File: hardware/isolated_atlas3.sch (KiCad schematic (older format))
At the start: 15 parts, among them J501 CONN_01X02, P5 ATLAS_DO_PROBE, U501 ADM3260, U502 ATLAS_DO

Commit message: Trying out some test points.
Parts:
- added J15, J16: CONN_01x02, conservify:TP_Pads_D1.5mm_1x2, symbol conservify:CONN_01x02
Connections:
- wire segments 78 -> 82
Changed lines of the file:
@@
 NoConn ~ 3650 3000
 NoConn ~ 5200 3000
+Text Label 8350 4500 0    60   ~ 0
+ISO_GND
+Text Label 8350 4400 0    60   ~ 0
+ISO_VCC
+Text Label 8350 4150 0    60   ~ 0
+ISO_SCL
+Text Label 8350 4250 0    60   ~ 0
+ISO_SDA
+Wire Wire Line
+	8350 4150 8750 4150
+Wire Wire Line
+	8750 4250 8350 4250
+Wire Wire Line
+	8350 4400 8750 4400
+Wire Wire Line
+	8750 4500 8350 4500
+$Comp
+L conservify:CONN_01x02 J?
+U 1 1 5C0F07A8
+P 8950 4150
+AR Path="/594C282A/5C0F07A8" Ref="J?"  Part="1"
+AR Path="/594C282C/5C0F07A8" Ref="J15"  Part="1"
+F 0 "J15" H 9029 4142 50  0000 L CNN
+F 1 "CONN_01x02" H 9029 4051 50  0000 L CNN
+F 2 "conservify:TP_Pads_D1.5mm_1x2" H 8950 4150 50  0001 C CNN
+F 3 "" H 8950 4150 50  0001 C CNN
+	1    8950 4150
+	1    0    0    -1
+$EndComp
+$Comp
+L conservify:CONN_01x02 J?
+U 1 1 5C0F07AF
+P 8950 4400
+AR Path="/594C282A/5C0F07AF" Ref="J?"  Part="1"
+AR Path="/594C282C/5C0F07AF" Ref="J16"  Part="1"
+F 0 "J16" H 9029 4392 50  0000 L CNN
+F 1 "CONN_01x02" H 9029 4301 50  0000 L CNN
+F 2 "conservify:TP_Pads_D1.5mm_1x2" H 8950 4400 50  0001 C CNN
+F 3 "" H 8950 4400 50  0001 C CNN
+	1    8950 4400
+	1    0    0    -1
+$EndComp
 $EndSCHEMATC

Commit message: Add orientation indicator to SWD fp.
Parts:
- J15, J16: Critical (none) -> (none); MFN (none) -> (none); MFP (none) -> (none); Notes (none) -> (none); Package (none) -> (none); SPN1 (none) -> (none); Source (none) -> ANY; Subsystem (none) -> (none); Supplier1 (none) -> (none)
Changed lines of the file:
@@
+	1    0    0    -1
+$EndComp
+$Comp
+L conservify:CONN_01x02 J?
+U 1 1 5C0F07A8
+P 8950 4150
+AR Path="/594C282A/5C0F07A8" Ref="J?"  Part="1"
+AR Path="/594C282C/5C0F07A8" Ref="J15"  Part="1"
+F 0 "J15" H 9029 4142 50  0000 L CNN
+F 1 "CONN_01x02" H 9029 4051 50  0000 L CNN
+F 2 "conservify:TP_Pads_D1.5mm_1x2" H 8950 4150 50  0001 C CNN
+F 3 "" H 8950 4150 50  0001 C CNN
+F 4 " " H 9029 4242 50  0001 C CNN "Critical"
+F 5 " " H 9029 4242 50  0001 C CNN "MFN"
+F 6 " " H 9029 4242 50  0001 C CNN "MFP"
+F 7 " " H 9029 4242 50  0001 C CNN "Notes"
+F 8 " " H 9029 4242 50  0001 C CNN "Package"
+F 9 " " H 9029 4242 50  0001 C CNN "SPN1"
+F 10 "ANY" H 9029 4242 50  0001 C CNN "Source"
+F 11 " " H 9029 4242 50  0001 C CNN "Subsystem"
+F 12 " " H 9029 4242 50  0001 C CNN "Supplier1"
+	1    8950 4150
+	1    0    0    -1
+$EndComp
+$Comp
+L conservify:CONN_01x02 J?
+U 1 1 5C0F07AF
+P 8950 4400
+AR Path="/594C282A/5C0F07AF" Ref="J?"  Part="1"
+AR Path="/594C282C/5C0F07AF" Ref="J16"  Part="1"
+F 0 "J16" H 9029 4392 50  0000 L CNN
+F 1 "CONN_01x02" H 9029 4301 50  0000 L CNN
+F 2 "conservify:TP_Pads_D1.5mm_1x2" H 8950 4400 50  0001 C CNN
+F 3 "" H 8950 4400 50  0001 C CNN
+F 4 " " H 9029 4492 50  0001 C CNN "Critical"
+F 5 " " H 9029 4492 50  0001 C CNN "MFN"
+F 6 " " H 9029 4492 50  0001 C CNN "MFP"
+F 7 " " H 9029 4492 50  0001 C CNN "Notes"
+F 8 " " H 9029 4492 50  0001 C CNN "Package"
+F 9 " " H 9029 4492 50  0001 C CNN "SPN1"
+F 10 "ANY" H 9029 4492 50  0001 C CNN "Source"
+F 11 " " H 9029 4492 50  0001 C CNN "Subsystem"
+F 12 " " H 9029 4492 50  0001 C CNN "Supplier1"
+	1    8950 4400
 	1    0    0    -1
 $EndComp
@@
 Text Label 9450 2900 0    60   ~ 0
 DO_PGND
+Text Label 8350 4500 0    60   ~ 0
+ISO_GND
+Text Label 8350 4400 0    60   ~ 0
+ISO_VCC
+Text Label 8350 4150 0    60   ~ 0
+ISO_SCL
+Text Label 8350 4250 0    60   ~ 0
+ISO_SDA
 Wire Wire Line
 	5200 3300 5350 3300
@@
 Wire Wire Line
 	6900 2500 7400 2500
+Wire Wire Line
+	8350 4150 8750 4150
+Wire Wire Line
+	8750 4250 8350 4250
+Wire Wire Line
+	8350 4400 8750 4400
+Wire Wire Line
+	8750 4500 8350 4500
 Connection ~ 5350 3500
 Connection ~ 5350 3400
@@
 NoConn ~ 3650 3000
 NoConn ~ 5200 3000
-Text Label 8350 4500 0    60   ~ 0
-ISO_GND
-Text Label 8350 4400 0    60   ~ 0
-ISO_VCC
-Text Label 8350 4150 0    60   ~ 0
-ISO_SCL
-Text Label 8350 4250 0    60   ~ 0
-ISO_SDA
-Wire Wire Line
-	8350 4150 8750 4150
-Wire Wire Line
-	8750 4250 8350 4250
-Wire Wire Line
-	8350 4400 8750 4400
-Wire Wire Line
-	8750 4500 8350 4500
-$Comp
-L conservify:CONN_01x02 J?
-U 1 1 5C0F07A8
-P 8950 4150
-AR Path="/594C282A/5C0F07A8" Ref="J?"  Part="1"
-AR Path="/594C282C/5C0F07A8" Ref="J15"  Part="1"
-F 0 "J15" H 9029 4142 50  0000 L CNN
-F 1 "CONN_01x02" H 9029 4051 50  0000 L CNN
-F 2 "conservify:TP_Pads_D1.5mm_1x2" H 8950 4150 50  0001 C CNN
-F 3 "" H 8950 4150 50  0001 C CNN
-	1    8950 4150
-	1    0    0    -1
-$EndComp
-$Comp
-L conservify:CONN_01x02 J?
-U 1 1 5C0F07AF
-P 8950 4400
-AR Path="/594C282A/5C0F07AF" Ref="J?"  Part="1"
-AR Path="/594C282C/5C0F07AF" Ref="J16"  Part="1"
-F 0 "J16" H 9029 4392 50  0000 L CNN
-F 1 "CONN_01x02" H 9029 4301 50  0000 L CNN
-F 2 "conservify:TP_Pads_D1.5mm_1x2" H 8950 4400 50  0001 C CNN
-F 3 "" H 8950 4400 50  0001 C CNN
-	1    8950 4400
-	1    0    0    -1
-$EndComp
 $EndSCHEMATC

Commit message: Started transition to 4 layer board
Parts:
- removed J15, J16: CONN_01x02, conservify:TP_Pads_D1.5mm_1x2, symbol conservify:CONN_01x02
- C501, C502, C503, C504, C505, C506: symbol conservify:CAPACITOR_CERAMIC -> fk-atlas-rescue:CAPACITOR_CERAMIC-conservify
- J501: symbol conservify:CONN_01x02 -> fk-atlas-rescue:CONN_01x02-conservify
- P5: symbol conservify:ATLAS_WATER_PROBE -> fk-atlas-rescue:ATLAS_WATER_PROBE-conservify
- R501, R502, R503, R504, R505: symbol conservify:R -> fk-atlas-rescue:R-conservify
- U501: symbol conservify:ADM3260 -> fk-atlas-rescue:ADM3260-conservify
- U502: footprint conservify:ATLAS_SENSOR_BOARD_OEM -> conservify:ATLAS_SENSOR_BOARD_COMBO; symbol conservify:ATLAS_SENSOR -> fk-atlas-rescue:ATLAS_SENSOR-conservify
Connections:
- wire segments 82 -> 78
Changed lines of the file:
@@
 $EndDescr
 $Comp
-L conservify:ADM3260 U501
+L fk-atlas-rescue:ADM3260-conservify U501
 U 1 1 594C2CF0
 P 4400 2900
@@
 $EndComp
 $Comp
-L conservify:CAPACITOR_CERAMIC C503
+L fk-atlas-rescue:CAPACITOR_CERAMIC-conservify C503
 U 1 1 594C2CF5
 P 5650 3800
@@
 $EndComp
 $Comp
-L conservify:CAPACITOR_CERAMIC C504
+L fk-atlas-rescue:CAPACITOR_CERAMIC-conservify C504
 U 1 1 594C2CF9
 P 5650 4100
@@
 $EndComp
 $Comp
-L conservify:CAPACITOR_CERAMIC C505
+L fk-atlas-rescue:CAPACITOR_CERAMIC-conservify C505
 U 1 1 594C2CFC
 P 5650 4400
@@
 $EndComp
 $Comp
-L conservify:CAPACITOR_CERAMIC C506
+L fk-atlas-rescue:CAPACITOR_CERAMIC-conservify C506
 U 1 1 594C2D00
 P 5650 4650
@@
 $EndComp
 $Comp
-L conservify:CAPACITOR_CERAMIC C501
+L fk-atlas-rescue:CAPACITOR_CERAMIC-conservify C501
 U 1 1 5948D5F5
 P 2900 3800
@@
 $EndComp
 $Comp
-L conservify:CAPACITOR_CERAMIC C502
+L fk-atlas-rescue:CAPACITOR_CERAMIC-conservify C502
 U 1 1 5948D68D
 P 2900 4100
@@
 $EndComp
 $Comp
-L conservify:R R501
+L fk-atlas-rescue:R-conservify R501
 U 1 1 594C2D0D
 P 5650 3300
@@
 $EndComp
 $Comp
-L conservify:R R502
+L fk-atlas-rescue:R-conservify R502
 U 1 1 594C2D11
 P 6250 2700
@@
 $EndComp
 $Comp
-L conservify:R R504
+L fk-atlas-rescue:R-conservify R504
 U 1 1 594C2D15
 P 6700 2700
@@
 $EndComp
 $Comp
-L conservify:R R503
+L fk-atlas-rescue:R-conservify R503
 U 1 1 594C2D19
 P 6300 3250
@@
 $EndComp
 $Comp
-L conservify:R R505
+L fk-atlas-rescue:R-conservify R505
 U 1 1 594C2D1D
 P 6800 3250
@@
 $EndComp
 $Comp
-L conservify:VCC #PWR063
+L fk-atlas-rescue:VCC-conservify #PWR063
 U 1 1 5948EDC0
 P 2450 3750
@@
 $EndComp
 $Comp
-L conservify:VCC #PWR064
+L fk-atlas-rescue:VCC-conservify #PWR064
 U 1 1 5948EDF6
 P 2450 2350
@@
 $EndComp
 $Comp
-L conservify:ATLAS_SENSOR U502
+L fk-atlas-rescue:ATLAS_SENSOR-conservify U502
 U 1 1 594C2D34
 P 8550 2900
 F 0 "U502" H 8100 2550 60  0000 C CNN
 F 1 "ATLAS_DO" H 8600 2850 60  0000 C CNN
-F 2 "conservify:ATLAS_SENSOR_BOARD_OEM" H 8550 2900 60  0001 C CNN
+F 2 "conservify:ATLAS_SENSOR_BOARD_COMBO" H 8550 2900 60  0001 C CNN
 F 3 "" H 8550 2900 60  0001 C CNN
 F 4 " " H 8100 2650 50  0001 C CNN "Critical"
@@
 $EndComp
 $Comp
-L conservify:CONN_01x02 J501
+L fk-atlas-rescue:CONN_01x02-conservify J501
 U 1 1 594D403D
 P 10050 2900
@@
 $EndComp
 $Comp
-L conservify:ATLAS_WATER_PROBE P5
+L fk-atlas-rescue:ATLAS_WATER_PROBE-conservify P5
 U 1 1 59D2A6F4
 P 8800 3600
@@
 $EndComp
 $Comp
-L conservify:PWR_FLAG #FLG0108
+L fk-atlas-rescue:PWR_FLAG-conservify #FLG0108
 U 1 1 5BCDA7BC
 P 7400 4900
@@
 F 3 "~" H 7400 4900 50  0001 C CNN
 	1    7400 4900
-	1    0    0    -1
-$EndComp
-$Comp
-L conservify:CONN_01x02 J?
-U 1 1 5C0F07A8
-P 8950 4150
-AR Path="/594C282A/5C0F07A8" Ref="J?"  Part="1"
-AR Path="/594C282C/5C0F07A8" Ref="J15"  Part="1"
-F 0 "J15" H 9029 4142 50  0000 L CNN
-F 1 "CONN_01x02" H 9029 4051 50  0000 L CNN
-F 2 "conservify:TP_Pads_D1.5mm_1x2" H 8950 4150 50  0001 C CNN
-F 3 "" H 8950 4150 50  0001 C CNN
-F 4 " " H 9029 4242 50  0001 C CNN "Critical"
-F 5 " " H 9029 4242 50  0001 C CNN "MFN"
-F 6 " " H 9029 4242 50  0001 C CNN "MFP"
-F 7 " " H 9029 4242 50  0001 C CNN "Notes"
-F 8 " " H 9029 4242 50  0001 C CNN "Package"
-F 9 " " H 9029 4242 50  0001 C CNN "SPN1"
-F 10 "ANY" H 9029 4242 50  0001 C CNN "Source"
-F 11 " " H 9029 4242 50  0001 C CNN "Subsystem"
-F 12 " " H 9029 4242 50  0001 C CNN "Supplier1"
-	1    8950 4150
-	1    0    0    -1
-$EndComp
-$Comp
-L conservify:CONN_01x02 J?
-U 1 1 5C0F07AF
-P 8950 4400
-AR Path="/594C282A/5C0F07AF" Ref="J?"  Part="1"
-AR Path="/594C282C/5C0F07AF" Ref="J16"  Part="1"
-F 0 "J16" H 9029 4392 50  0000 L CNN
-F 1 "CONN_01x02" H 9029 4301 50  0000 L CNN
-F 2 "conservify:TP_Pads_D1.5mm_1x2" H 8950 4400 50  0001 C CNN
-F 3 "" H 8950 4400 50  0001 C CNN
-F 4 " " H 9029 4492 50  0001 C CNN "Critical"
-F 5 " " H 9029 4492 50  0001 C CNN "MFN"
-F 6 " " H 9029 4492 50  0001 C CNN "MFP"
-F 7 " " H 9029 4492 50  0001 C CNN "Notes"
-F 8 " " H 9029 4492 50  0001 C CNN "Package"
-F 9 " " H 9029 4492 50  0001 C CNN "SPN1"
-F 10 "ANY" H 9029 4492 50  0001 C CNN "Source"
-F 11 " " H 9029 4492 50  0001 C CNN "Subsystem"
-F 12 " " H 9029 4492 50  0001 C CNN "Supplier1"
-	1    8950 4400
 	1    0    0    -1
 $EndComp
@@
 Text Label 9450 2900 0    60   ~ 0
 DO_PGND
-Text Label 8350 4500 0    60   ~ 0
-ISO_GND
-Text Label 8350 4400 0    60   ~ 0
-ISO_VCC
-Text Label 8350 4150 0    60   ~ 0
-ISO_SCL
-Text Label 8350 4250 0    60   ~ 0
-ISO_SDA
 Wire Wire Line
 	5200 3300 5350 3300
@@
 Wire Wire Line
 	6900 2500 7400 2500
-Wire Wire Line
-	8350 4150 8750 4150
-Wire Wire Line
-	8750 4250 8350 4250
-Wire Wire Line
-	8350 4400 8750 4400
-Wire Wire Line
-	8750 4500 8350 4500
 Connection ~ 5350 3500
 Connection ~ 5350 3400

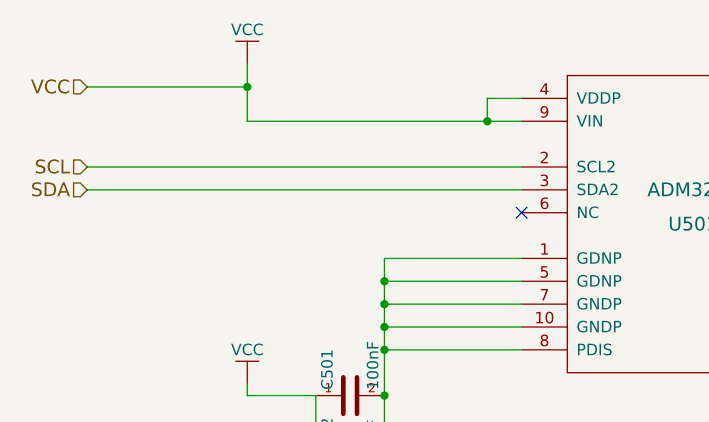
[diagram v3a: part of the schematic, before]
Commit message: Added pull up resistors and a debounce cap for the reset button
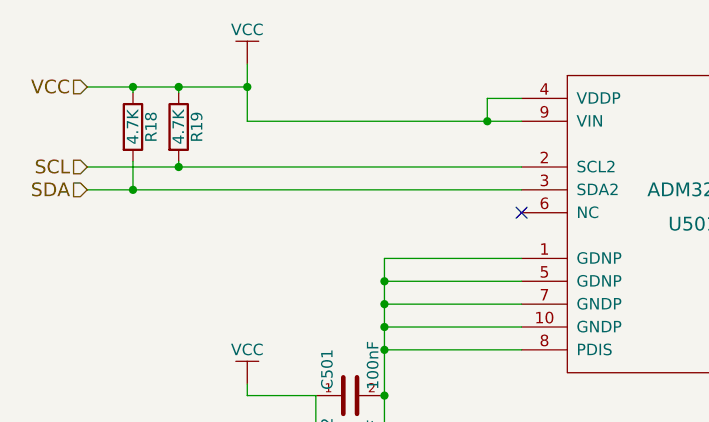
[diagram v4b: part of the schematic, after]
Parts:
- added R18, R19: 4.7K, conservify:RES-0603, symbol fk-atlas-rescue:R-conservify
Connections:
- net SCL: now also R19.2
- net SDA: now also R18.2
- net VCC: now also R18.1, R19.1
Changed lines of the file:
@@
 	2450 3800 2450 3750
 Wire Wire Line
-	1750 2800 3650 2800
+	1750 2800 2150 2800
 Wire Wire Line
-	1750 2900 3650 2900
+	1750 2900 1950 2900
 Wire Wire Line
-	1750 2450 2450 2450
+	1750 2450 1950 2450
 Wire Wire Line
 	5350 5000 7400 5000
@@
 NoConn ~ 3650 3000
 NoConn ~ 5200 3000
+$Comp
+L fk-atlas-rescue:R-conservify R18
+U 1 1 5C7DFDFD
+P 1950 2625
+F 0 "R18" V 2030 2625 50  0000 C CNN
+F 1 "4.7K" V 1950 2625 50  0000 C CNN
+F 2 "conservify:RES-0603" V 1880 2625 50  0001 C CNN
+F 3 "" H 1950 2625 50  0001 C CNN
+F 4 " " H 2030 2725 50  0001 C CNN "Critical"
+F 5 "Yageo" H 2030 2725 50  0001 C CNN "MFN"
+F 6 "AF0603JR-074K7L" H 2030 2725 50  0001 C CNN "MFP"
+F 7 " " H 2030 2725 50  0001 C CNN "Notes"
+F 8 " " H 2030 2725 50  0001 C CNN "Package"
+F 9 "ANY" H 2030 2725 50  0001 C CNN "Source"
+F 10 " " H 2030 2725 50  0001 C CNN "Subsystem"
+F 11 "mouser" H 2030 2725 50  0001 C CNN "Supplier1"
+F 12 "0" H 2030 2725 50  0001 C CNN "price"
+F 13 "603-AF0603JR-074K7L" H -4350 -625 50  0001 C CNN "spn1"
+F 14 "mouser" H -4350 -625 50  0001 C CNN "spn2"
+	1    1950 2625
+	1    0    0    -1
+$EndComp
+$Comp
+L fk-atlas-rescue:R-conservify R19
+U 1 1 5C7DFF29
+P 2150 2625
+F 0 "R19" V 2230 2625 50  0000 C CNN
+F 1 "4.7K" V 2150 2625 50  0000 C CNN
+F 2 "conservify:RES-0603" V 2080 2625 50  0001 C CNN
+F 3 "" H 2150 2625 50  0001 C CNN
+F 4 " " H 2230 2725 50  0001 C CNN "Critical"
+F 5 "Yageo" H 2230 2725 50  0001 C CNN "MFN"
+F 6 "AF0603JR-074K7L" H 2230 2725 50  0001 C CNN "MFP"
+F 7 " " H 2230 2725 50  0001 C CNN "Notes"
+F 8 " " H 2230 2725 50  0001 C CNN "Package"
+F 9 "ANY" H 2230 2725 50  0001 C CNN "Source"
+F 10 " " H 2230 2725 50  0001 C CNN "Subsystem"
+F 11 "mouser" H 2230 2725 50  0001 C CNN "Supplier1"
+F 12 "0" H 2230 2725 50  0001 C CNN "price"
+F 13 "603-AF0603JR-074K7L" H -4150 -625 50  0001 C CNN "spn1"
+F 14 "mouser" H -4150 -625 50  0001 C CNN "spn2"
+	1    2150 2625
+	1    0    0    -1
+$EndComp
+Wire Wire Line
+	1950 2475 1950 2450
+Connection ~ 1950 2450
+Wire Wire Line
+	1950 2450 2150 2450
+Wire Wire Line
+	1950 2775 1950 2900
+Connection ~ 1950 2900
+Wire Wire Line
+	1950 2900 3650 2900
+Wire Wire Line
+	2150 2775 2150 2800
+Connection ~ 2150 2800
+Wire Wire Line
+	2150 2800 3650 2800
+Wire Wire Line
+	2150 2475 2150 2450
+Connection ~ 2150 2450
+Wire Wire Line
+	2150 2450 2450 2450
 $EndSCHEMATC
